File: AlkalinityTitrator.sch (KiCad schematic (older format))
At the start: 44 parts, among them J1 Conn_01x16, J10 Screw_Terminal_01x02, J12 V_OFFSET, J14 Conn_01x02, J2 Raspberry_Pi_2_3, J3 Conn_01x08, J4 Screw_Terminal_01x04_titrator, J5 RF_Shield_Two_Pieces, J6 BNC_Jack, J7 SJ-43515TS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

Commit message: sleep is for losers. Did layout for Rev 3 board
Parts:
- removed J12: V_OFFSET, Connector_PinHeader_2.54mm:PinHeader_1x01_P2.54mm_Vertical, symbol Connector_Generic:Conn_01x01
- J1: footprint Titrator_Footprints:PinSocket_1x16_P2.54mm_Horizontal -> Titrator_Footprints:PinHeader_1x16_P2.54mm_Horizontal
- J14: footprint Titrator_Footprints:PinSocket_1x02_P2.54mm_Vertical -> Titrator_Footprints:PinHeader_1x02_P2.54mm_Horizontal
- J3: footprint Titrator_Footprints:PinSocket_1x08_P2.54mm_Horizontal -> Titrator_Footprints:PinHeader_1x08_P2.54mm_Horizontal
- J5: footprint Titrator_Footprints:44-CBSA-1.0X1.5X0.4 -> Titrator_Footprints:SMS-205_LeaderTech_RFShield
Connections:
- net GND: now also J2.39 (GND), U2.10 (GND); no longer J2.9 (GND)
- net PSU_GND: now also J2.9 (GND); no longer J2.39 (GND), U2.10 (GND)
- net at U2.11 (2B): now also J4.4 (1B); no longer J4.1 (2B)
- net at U2.12 (2A): now also J4.3 (1A); no longer J4.2 (2A)
- net at U2.13 (1A): now also J4.2 (2A); no longer J4.3 (1A)
- net at U2.14 (1B): now also J4.1 (2B); no longer J4.4 (1B)
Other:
- note added: "Raspberry Pi Mounting Holes +2\n(Non-Plated Through Holes)"
- note removed: "Raspberry Pi Mounting Holes\n(Non-Plated Through Holes)"
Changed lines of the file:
@@
 L titrator:Screw_Terminal_01x04_titrator J4
 U 1 1 5F1C81E1
-P 3675 6225
-F 0 "J4" H 3625 6450 50  0000 L CNN
-F 1 "Screw_Terminal_01x04_titrator" H 3525 5900 50  0000 L CNN
-F 2 "Titrator_Footprints:TerminalBlock_bornier-4_P5.08mm" H 3675 6225 50  0001 C CNN
-F 3 "~" H 3675 6225 50  0001 C CNN
-	1    3675 6225
-	1    0    0    -1
+P 3675 6325
+F 0 "J4" H 3625 6550 50  0000 L CNN
+F 1 "Screw_Terminal_01x04_titrator" H 3575 6625 50  0000 L CNN
+F 2 "Titrator_Footprints:TerminalBlock_bornier-4_P5.08mm" H 3675 6325 50  0001 C CNN
+F 3 "~" H 3675 6325 50  0001 C CNN
+	1    3675 6325
+	1    0    0    1
 $EndComp
 Wire Wire Line
@@
 F 0 "J14" H 9505 5417 50  0000 L CNN
 F 1 "Conn_01x02" H 9505 5326 50  0000 L CNN
-F 2 "Titrator_Footprints:PinSocket_1x02_P2.54mm_Vertical" H 9425 5425 50  0001 C CNN
+F 2 "Titrator_Footprints:PinHeader_1x02_P2.54mm_Horizontal" H 9425 5425 50  0001 C CNN
 F 3 "~" H 9425 5425 50  0001 C CNN
 	1    9425 5425
@@
 Text Notes 6225 1650 0    50   ~ 0
 Level-shifted Configuration\nReference electrode level shifted \nby 2.5V to allow for single-supply
-$Comp
-L Connector_Generic:Conn_01x01 J12
-U 1 1 606D75F0
-P 9450 4025
-F 0 "J12" H 9375 4200 50  0000 L CNN
-F 1 "V_OFFSET" H 9275 4125 50  0000 L CNN
-F 2 "Connector_PinHeader_2.54mm:PinHeader_1x01_P2.54mm_Vertical" H 9450 4025 50  0001 C CNN
-F 3 "~" H 9450 4025 50  0001 C CNN
-	1    9450 4025
-	1    0    0    -1
-$EndComp
 Text Notes 9300 2525 0    50   ~ 0
 MAKE THESE \nCONNECTIONS\nVERY SHORT \nON PCB
@@
 F 0 "J5" H 10400 1875 50  0000 L CNN
 F 1 "RF_Shield_Two_Pieces" H 10050 1775 50  0000 L CNN
-F 2 "Titrator_Footprints:44-CBSA-1.0X1.5X0.4" H 10450 1125 50  0001 C CNN
+F 2 "Titrator_Footprints:SMS-205_LeaderTech_RFShield" H 10450 1125 50  0001 C CNN
 F 3 "https://leadertechinc.com/product/40-series/" H 10450 1125 50  0001 C CNN
 	1    10450 1225
@@
 PSU_AGND
 Text Label 3750 1475 3    50   ~ 0
-PSU_GND
-Text Label 2975 6025 0    50   ~ 0
 PSU_GND
 $Comp
@@
 F 0 "J3" H 4430 7217 50  0000 L CNN
 F 1 "Conn_01x08" H 4430 7126 50  0000 L CNN
-F 2 "Titrator_Footprints:PinSocket_1x08_P2.54mm_Horizontal" H 4350 7225 50  0001 C CNN
+F 2 "Titrator_Footprints:PinHeader_1x08_P2.54mm_Horizontal" H 4350 7225 50  0001 C CNN
 F 3 "~" H 4350 7225 50  0001 C CNN
 	1    4350 7225
@@
 	2000 5000 2000 5100
 Wire Wire Line
-	1500 5000 1500 5100
-Wire Wire Line
 	1800 5100 1900 5100
 Connection ~ 1800 5100
@@
 	1800 5100 1700 5100
 Connection ~ 1700 5100
-Wire Wire Line
-	1500 5100 1600 5100
 Wire Wire Line
 	1600 5100 1700 5100
@@
 	1    0    0    -1
 $EndComp
-Text Label 2100 5000 0    50   ~ 0
+Text Label 1500 5200 3    50   ~ 0
 PSU_GND
 Wire Wire Line
@@
 F 0 "J1" V 1850 7571 50  0000 C CNN
 F 1 "Conn_01x16" V 1941 7571 50  0000 C CNN
-F 2 "Titrator_Footprints:PinSocket_1x16_P2.54mm_Horizontal" H 1725 7625 50  0001 C CNN
+F 2 "Titrator_Footprints:PinHeader_1x16_P2.54mm_Horizontal" H 1725 7625 50  0001 C CNN
 F 3 "~" H 1725 7625 50  0001 C CNN
 	1    1725 7625
@@
 NoConn ~ 1725 7425
 NoConn ~ 1825 7425
-Wire Wire Line
-	1400 5100 1500 5100
 Connection ~ 1400 5100
-Connection ~ 1500 5100
 NoConn ~ 10025 5850
 NoConn ~ 10025 4850
@@
 	550  1100 550  550
 Text Notes 700  1275 0    50   ~ 0
-Raspberry Pi Mounting Holes\n(Non-Plated Through Holes)
+Raspberry Pi Mounting Holes +2\n(Non-Plated Through Holes)
 Wire Wire Line
 	4900 5700 4900 5575
@@
 IMPORTANT!\nCircuitPython uses CE0 and \nCE1 for chip enable magic. \nDo not use them as chip \nenables! Any other GPIO pin \ncan act as a chip enable \ninstead.
 Wire Wire Line
-	9000 3825 9000 4025
-Wire Wire Line
-	9000 4025 9250 4025
-Connection ~ 9000 4025
-Wire Wire Line
-	9000 4025 9000 4175
-Wire Wire Line
 	8125 4200 8125 4100
 Wire Wire Line
@@
 Text Notes 7150 800  0    50   ~ 0
 Schottky Diodes between the ground planes will only\npass signals greater than 0.3V. This keeps them from\ndrifting too far apart while preventing noise from passing
+Wire Wire Line
+	1400 5100 1600 5100
+Wire Wire Line
+	2000 5100 2100 5100
+Wire Wire Line
+	2100 5100 2100 5000
+Connection ~ 2000 5100
+Wire Wire Line
+	1500 5000 1500 5200
+$Comp
+L power:GND #PWR0102
+U 1 1 610412AA
+P 2975 6025
+F 0 "#PWR0102" H 2975 5775 50  0001 C CNN
+F 1 "GND" H 2980 5852 50  0000 C CNN
+F 2 "" H 2975 6025 50  0001 C CNN
+F 3 "" H 2975 6025 50  0001 C CNN
+	1    2975 6025
+	0    -1   -1   0
+$EndComp
+Wire Wire Line
+	9000 3825 9000 4175
 $EndSCHEMATC

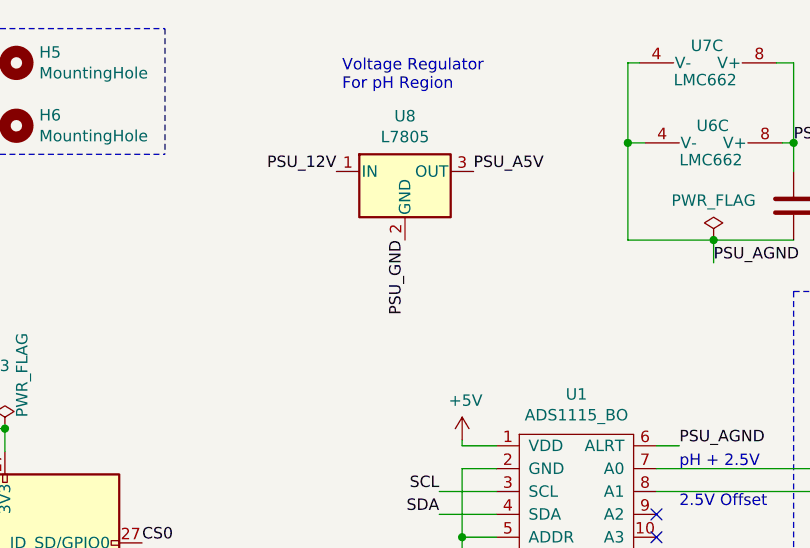
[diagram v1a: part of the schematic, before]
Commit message: Finished Rev3, added silkscreen, added voltage reference capacitors, generated gerbers and drills
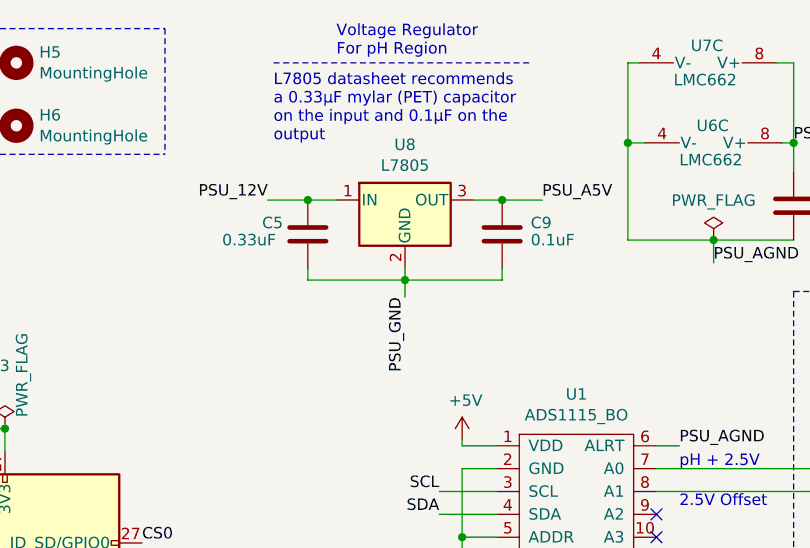
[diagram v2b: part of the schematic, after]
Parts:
- added C5: 0.33uF, Titrator_Footprints:C_Rect_L7.2mm_W3.5mm_P5.00mm_FKS2_FKP2_MKS2_MKP2, symbol Device:C
- added C9: 0.1uF, Titrator_Footprints:C_Rect_L7.2mm_W3.5mm_P5.00mm_FKS2_FKP2_MKS2_MKP2, symbol Device:C
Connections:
- net PSU_12V: now also C5.1
- net PSU_A5V: now also C9.1
- net PSU_GND: now also C5.2, C9.2
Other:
- note added: "L7805 datasheet recommends \na 0.33μF mylar (PET) capacitor\non the input and 0.1μF on the\noutput"
- moved on the sheet: U8
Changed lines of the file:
@@
 L Regulator_Linear:L7805 U8
 U 1 1 603CB9D6
-P 3750 1175
-F 0 "U8" H 3750 1417 50  0000 C CNN
-F 1 "L7805" H 3750 1326 50  0000 C CNN
-F 2 "Titrator_Footprints:78XXS" H 3775 1025 50  0001 L CIN
-F 3 "http://www.st.com/content/ccc/resource/technical/document/datasheet/41/4f/b3/b0/12/d4/47/88/CD00000444.pdf/files/CD00000444.pdf/jcr:content/translations/en.CD00000444.pdf" H 3750 1125 50  0001 C CNN
-	1    3750 1175
-	1    0    0    -1
-$EndComp
-Text Label 4050 1175 0    50   ~ 0
+P 3750 1300
+F 0 "U8" H 3750 1542 50  0000 C CNN
+F 1 "L7805" H 3750 1451 50  0000 C CNN
+F 2 "Titrator_Footprints:78XXS" H 3775 1150 50  0001 L CIN
+F 3 "http://www.st.com/content/ccc/resource/technical/document/datasheet/41/4f/b3/b0/12/d4/47/88/CD00000444.pdf/files/CD00000444.pdf/jcr:content/translations/en.CD00000444.pdf" H 3750 1250 50  0001 C CNN
+	1    3750 1300
+	1    0    0    -1
+$EndComp
+Text Label 4350 1300 0    50   ~ 0
 PSU_A5V
-Text Label 3450 1175 2    50   ~ 0
+Text Label 3150 1300 2    50   ~ 0
 PSU_12V
 Wire Notes Line
@@
 Text Label 8125 4200 2    50   ~ 0
 PSU_AGND
-Text Label 3750 1475 3    50   ~ 0
+Text Label 3750 1725 3    50   ~ 0
 PSU_GND
 $Comp
@@
 Text Notes 6075 3100 0    50   ~ 0
 1Hz Cutoff  Active \nLow Pass Filter
-Text Notes 3475 825  0    50   ~ 0
+Text Notes 3450 675  0    50   ~ 0
 Voltage Regulator\nFor pH Region
 Text Notes 6800 3500 0    50   ~ 0
@@
 Wire Wire Line
 	9000 3825 9000 4175
+$Comp
+L Device:C C9
+U 1 1 60C5A1DE
+P 4175 1450
+F 0 "C9" H 4300 1500 50  0000 L CNN
+F 1 "0.1uF" H 4300 1425 50  0000 L CNN
+F 2 "Titrator_Footprints:C_Rect_L7.2mm_W3.5mm_P5.00mm_FKS2_FKP2_MKS2_MKP2" H 4213 1300 50  0001 C CNN
+F 3 "~" H 4175 1450 50  0001 C CNN
+	1    4175 1450
+	1    0    0    -1
+$EndComp
+$Comp
+L Device:C C5
+U 1 1 60C5B39D
+P 3325 1450
+F 0 "C5" H 3125 1500 50  0000 L CNN
+F 1 "0.33uF" H 2950 1425 50  0000 L CNN
+F 2 "Titrator_Footprints:C_Rect_L7.2mm_W3.5mm_P5.00mm_FKS2_FKP2_MKS2_MKP2" H 3363 1300 50  0001 C CNN
+F 3 "~" H 3325 1450 50  0001 C CNN
+	1    3325 1450
+	1    0    0    -1
+$EndComp
+Wire Wire Line
+	3150 1300 3325 1300
+Wire Wire Line
+	3325 1300 3450 1300
+Connection ~ 3325 1300
+Wire Wire Line
+	3750 1600 3750 1650
+Wire Wire Line
+	3325 1600 3325 1650
+Wire Wire Line
+	3325 1650 3750 1650
+Connection ~ 3750 1650
+Wire Wire Line
+	3750 1650 3750 1725
+Wire Wire Line
+	3750 1650 4175 1650
+Wire Wire Line
+	4175 1650 4175 1600
+Wire Wire Line
+	4050 1300 4175 1300
+Wire Wire Line
+	4175 1300 4350 1300
+Connection ~ 4175 1300
+Text Notes 3175 1050 0    50   ~ 0
+L7805 datasheet recommends \na 0.33μF mylar (PET) capacitor\non the input and 0.1μF on the\noutput
+Wire Notes Line
+	3175 700  4300 700
 $EndSCHEMATC

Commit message: Cleaning up repo
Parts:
- C4: value .1uF -> 0.1uF
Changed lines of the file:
@@
 P 9725 4275
 F 0 "C4" H 9840 4321 50  0000 L CNN
-F 1 ".1uF" H 9840 4230 50  0000 L CNN
+F 1 "0.1uF" H 9840 4230 50  0000 L CNN
 F 2 "Capacitor_THT:C_Disc_D3.8mm_W2.6mm_P2.50mm" H 9763 4125 50  0001 C CNN
 F 3 "~" H 9725 4275 50  0001 C CNN
